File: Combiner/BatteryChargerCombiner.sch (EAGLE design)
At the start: 148 parts, among them Q1 DMN6040SSD-13, Q2 DMN6040SSD-13, Q3 DMN6040SSD-13, Q4 DMN6040SSD-13, Q5 DMP4047SSD-13, Q6 220mA/50V/3.5Ω, Q7 220mA/50V/3.5Ω, U1 BQ24650, U10 TS7211, U11 MIC5219 3.3V, U12 MKR1000-SMD, U13 STWD100, U2 BQ28Z610, U3 BQ28Z610, U4 BQ24650, U5 TCA9543A, U6 WE-78, U7 WE-78, U8 74AHC1G07DBV, U9 74AUC1G06DBV

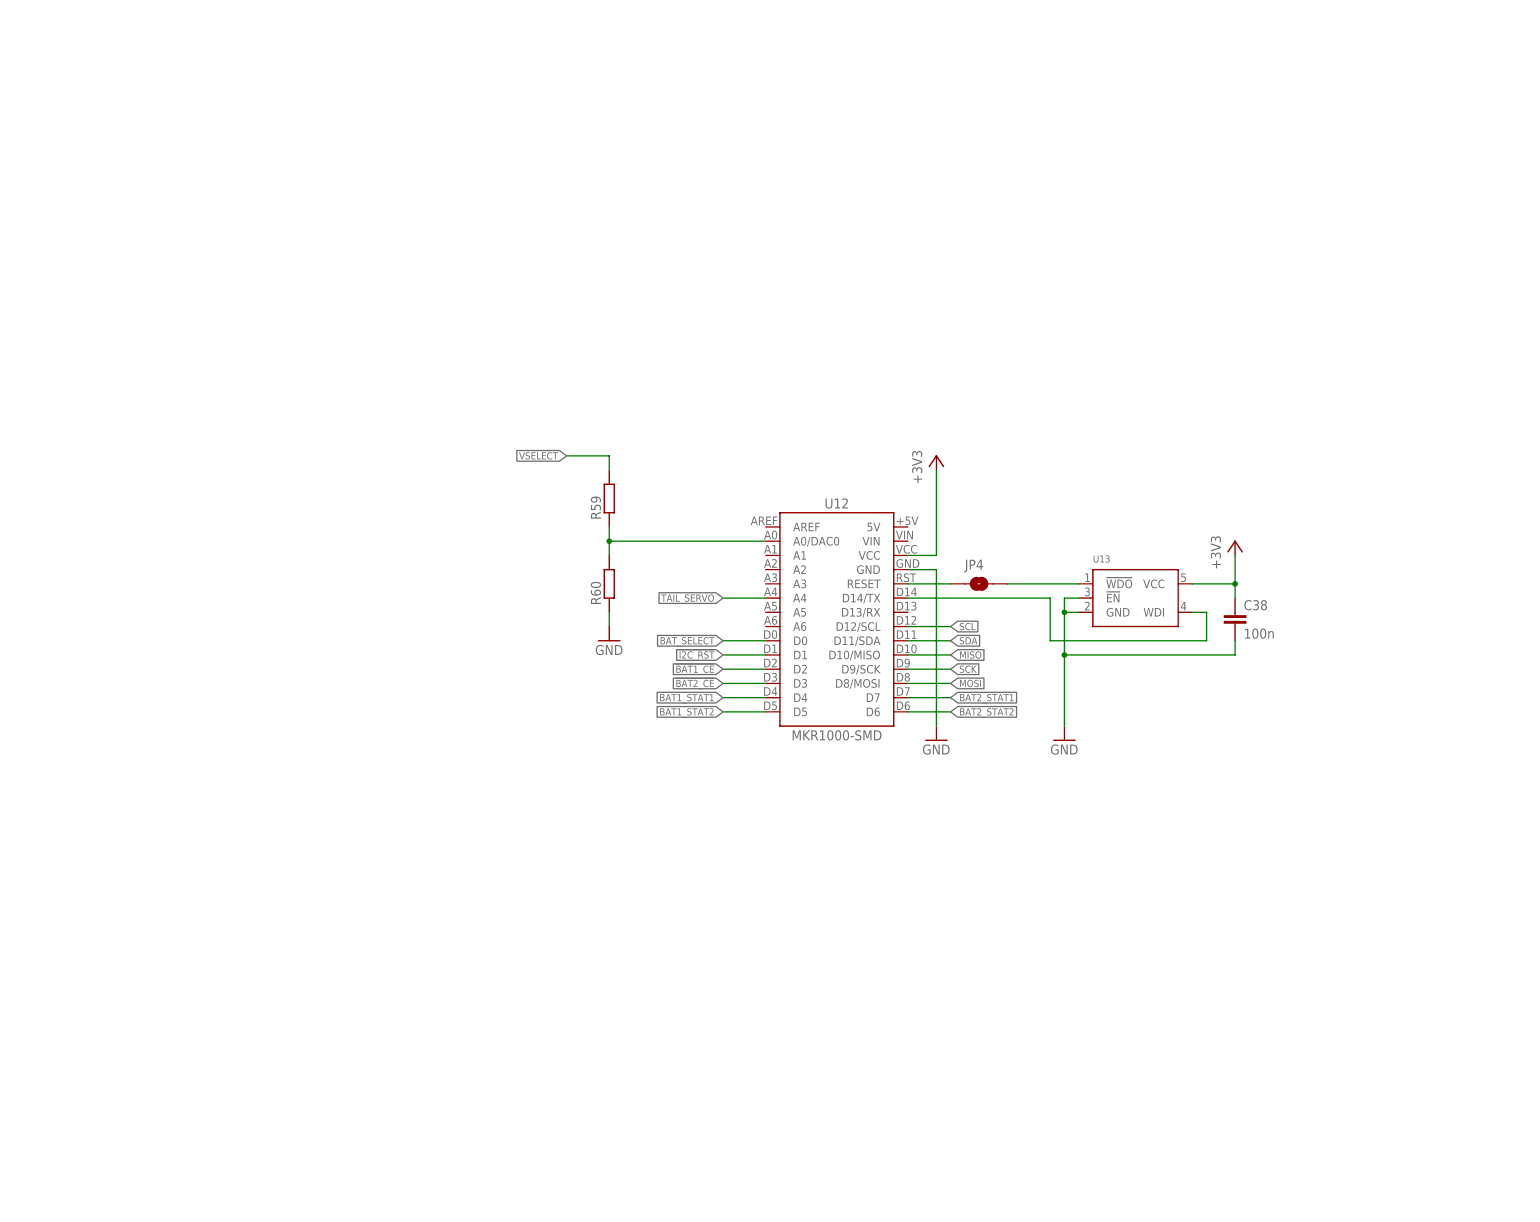
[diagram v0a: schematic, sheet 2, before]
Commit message: Added temp sensor inputs, power switches, and mounting holes
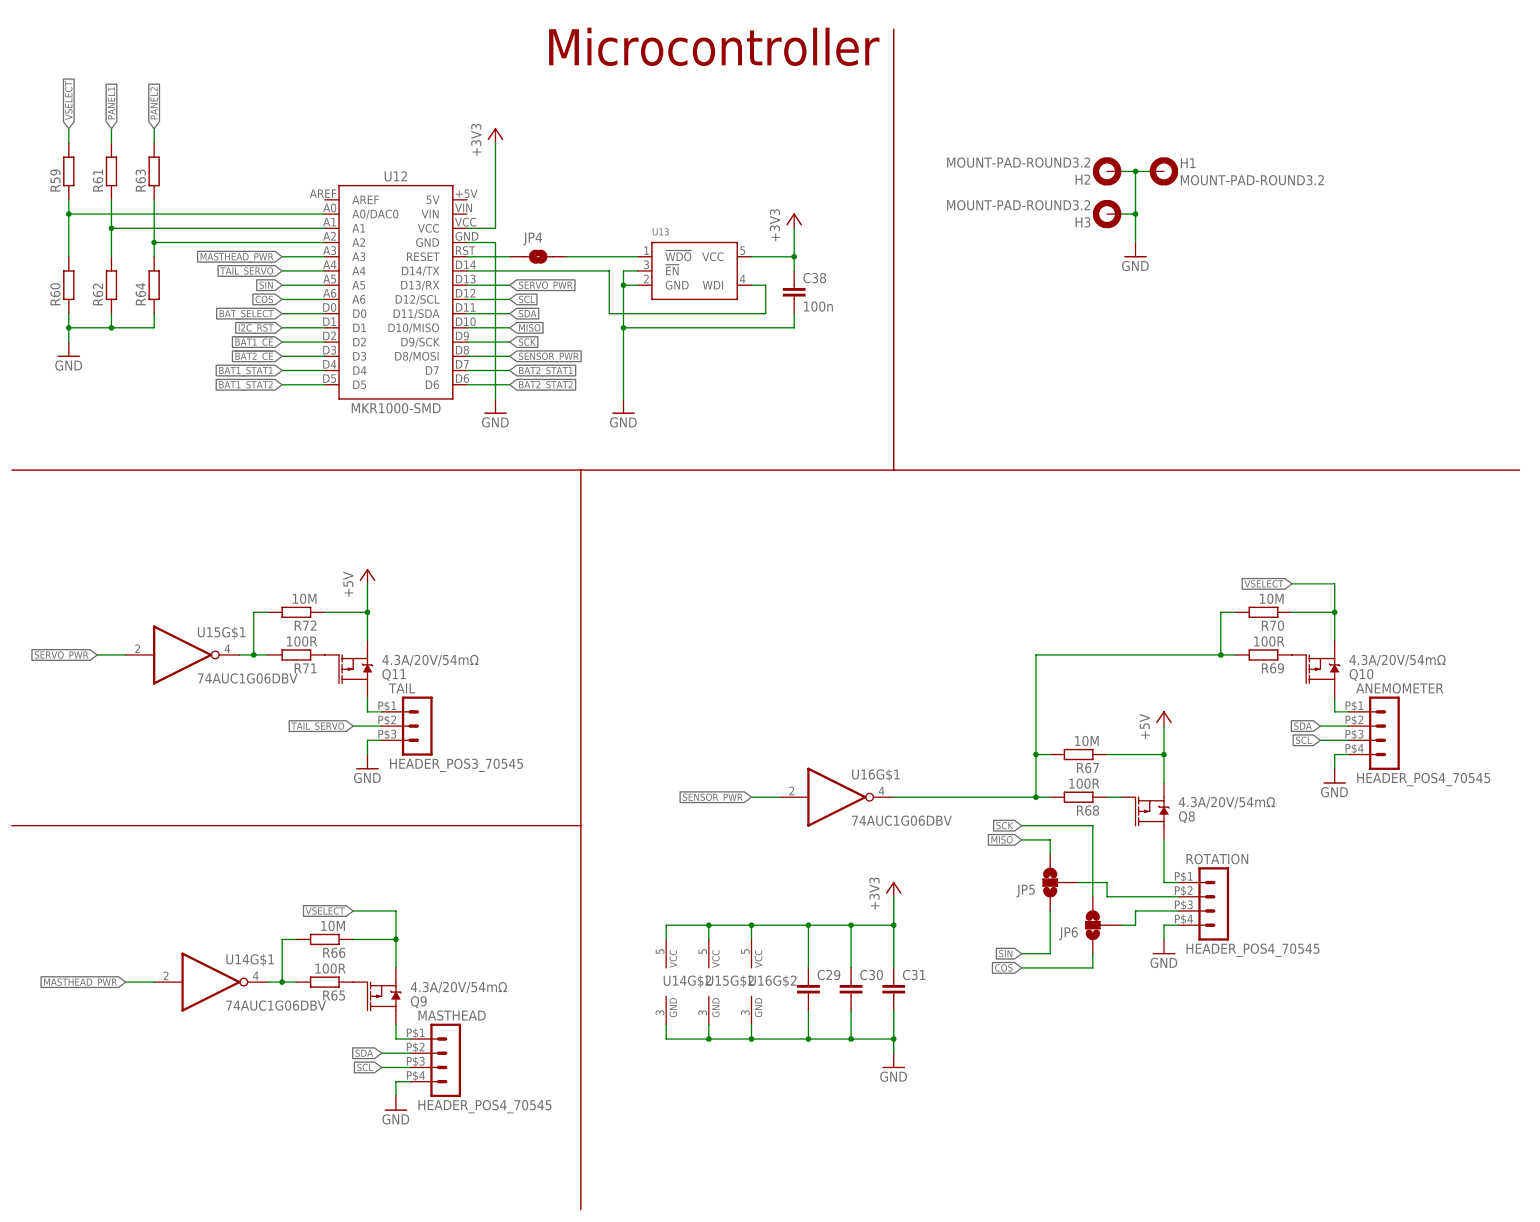
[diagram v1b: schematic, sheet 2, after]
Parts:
- removed JP3: JUMPER-SMT_3_NO_SILK, SparkFun-Jumpers:JUMPER-SMT_3_NO_SILK
- added C29, C30, C31: (no value), resistor:C-EUC0603
- added H1, H2, H3: MOUNT-PAD-ROUND3.2, holes:MOUNT-PAD-ROUND3.2
- added JP5, JP6: JUMPER-SMT_3_NO_SILK, SparkFun-Jumpers:JUMPER-SMT_3_NO_SILK
- added MASTHEAD: HEADER_POS4_70545, con-molex-c-grid-sl:HEADER_POS4_70545
- added Q10, Q11, Q8, Q9: 4.3A/20V/54mΩ, SparkFun-DiscreteSemi:MOSFET_PCH-IRLML2244
- added R61, R62, R63, R64: (no value), resistor:R-EU_R0603
- added R65, R68, R69, R71: 100R, resistor:R-EU_R0603
- added R66, R67, R70, R72: 10M, resistor:R-EU_R0603
- added U14, U15, U16: 74AUC1G06DBV, 74xx-little-us:74AUC1G06DBV
- BAT1_TS, BAT2_TS: value TPPAD1-13Y -> HEADER_POS3_70545; device testpad:TPPAD1-13Y -> con-molex-c-grid-sl:HEADER_POS3_70545
- ROTATION: value HEADER_POS5_70545 -> HEADER_POS4_70545; device con-molex-c-grid-sl:HEADER_POS5_70545 -> con-molex-c-grid-sl:HEADER_POS4_70545
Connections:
- removed net BAT1_TS: U2.TS1
- removed net BAT2_TS: U3.TS1
- removed net MOSI: ROTATION.2, U12.D8/MOSI
- removed net TS1: BAT1_TS.TP, R5.1, R6.2, U1.TS
- removed net TS2: BAT2_TS.TP, R16.1, R17.2, U4.TS
- new net BAT1_TS1: BAT1_TS.1, R5.1, R6.2, U1.TS
- new net BAT1_TS2: BAT1_TS.2, U2.TS1
- new net BAT2_TS1: BAT2_TS.1, R16.1, R17.2, U4.TS
- new net BAT2_TS2: BAT2_TS.2, U3.TS1
- new net COS: JP6.1, U12.A6
- new net MASTHEAD_PWR: U12.A3, U14G$1.I
- new net N$47: JP6.2, ROTATION.3
- new net N$49: JP5.2, ROTATION.2
- new net N$53: Q8.G, R68.1
- new net N$56: R63.1, R64.2, U12.A2
- new net N$58: MASTHEAD.1, Q9.D
- new net N$63: Q9.G, R65.1
- new net N$66: ANEMOMETER.1, Q10.D
- new net N$67: Q10.G, R69.1
- new net N$69: R67.2, R68.2, R69.2, R70.2, U16G$1.O
- new net N$70: Q11.D, TAIL.1
- new net N$71: Q11.G, R71.1
- new net N$72: R71.2, R72.2, U15G$1.O
- new net PANEL1: D1.A, PANEL1_POS.TP, R1.2, R61.2
- new net PANEL2: D2.A, PANEL2_POS.TP, R13.2, R63.2
- new net SENSOR_PWR: U12.D8/MOSI, U16G$1.I
- new net SERVO_PWR: U12.D13/RX, U15G$1.I
- new net SIN: JP5.1, U12.A5
- net +3V3: now also C29.1, C30.1, C31.1, U14G$2.VCC, U15G$2.VCC, U16G$2.VCC; no longer JP3.1
- net +5V: now also Q11.S, Q8.S, R67.1, R72.1; no longer JP3.3, TAIL.1
- net GND: now also BAT1_TS.3, BAT2_TS.3, C29.2, C30.2, C31.2, H1.MOUNT, H2.MOUNT, H3.MOUNT, MASTHEAD.4, R62.1, R64.1, ROTATION.4, U14G$2.GND, U15G$2.GND, U16G$2.GND; no longer ROTATION.5
- net MISO: now also JP5.3; no longer ROTATION.4
- net N$14: now also R61.1, R62.2, U12.A1; no longer D2.A, PANEL2_POS.TP, R13.2
- net N$2: now also Q8.D, ROTATION.1; no longer D1.A, PANEL1_POS.TP, R1.2
- net N$64: now also R65.2, R66.2, U14G$1.O; no longer JP3.2, ROTATION.1
- net SCK: now also JP6.3; no longer ROTATION.3
- net SCL: now also MASTHEAD.3
- net SDA: now also MASTHEAD.2
- net VSELECT: now also Q10.S, Q9.S, R66.1, R70.1; no longer ANEMOMETER.1
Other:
- note added: "Microcontroller"
- moved on the sheet: BAT1, BAT2, C38, JP4, PANEL1_NEG, PANEL1_POS, PANEL2_NEG, PANEL2_POS, PWR_OUT, R59, R60, U12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

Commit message: Silkscreen cleaned up; ready for test
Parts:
- removed JP4: JUMPER-SMT_2_NO_SILK, SparkFun-Jumpers:JUMPER-SMT_2_NO_SILK
- removed JP5, JP6: JUMPER-SMT_3_NO_SILK, SparkFun-Jumpers:JUMPER-SMT_3_NO_SILK
- added C32: 100n, resistor:C-EUC0603
- added R73, R74, R75, R76, R77, R78: (no value), resistor:R-EU_R0603
- added U17: LMV358, SparkFun-IC-Amplifiers:LMV358SOIC
- added WDT-RST: JUMPER-SMT_2_NO_SILK, SparkFun-Jumpers:JUMPER-SMT_2_NO_SILK
- C29, C30, C31: value (none) -> 100n
- SYSTEM: value HEADER_POS14_70545 -> HEADER_POS15_70545; device con-molex-c-grid-sl:HEADER_POS14_70545 -> con-molex-c-grid-sl:HEADER_POS15_70545
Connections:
- removed net N$14: R61.1, R62.2, U12.A1
- removed net N$47: JP6.2, ROTATION.3
- removed net N$49: JP5.2, ROTATION.2
- removed net N$56: R63.1, R64.2, U12.A2
- new net COS_IN: R75.2, ROTATION.3
- new net N$62: R73.1, R74.2, U17G1.-IN
- new net N$73: R75.1, R76.2, U17G2.-IN
- new net N$78: R77.1, R78.2, U17G1.+IN, U17G2.+IN
- new net PANEL1_DIV: R61.1, R62.2, SYSTEM.13, U12.A1
- new net PANEL2_DIV: R63.1, R64.2, SYSTEM.14, U12.A2
- new net SIN_IN: R73.2, ROTATION.2
- net +3V3: now also C32.1, R77.2, U17G3.P$V+
- net COS: now also R76.1, U17G2.OUT; no longer JP6.1
- net GND: now also C32.2, R78.1, SYSTEM.15, U17G3.P$V-; no longer SYSTEM.13, SYSTEM.14
- net MISO: no longer JP5.3
- net N$61: now also WDT-RST.1; no longer JP4.1
- net N$65: now also WDT-RST.2; no longer JP4.2
- net SCK: no longer JP6.3
- net SIN: now also R74.1, U17G1.OUT; no longer JP5.1
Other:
- note added: "Masthead Light"
- note added: "Power & Ground"
- note added: "Sensor Inputs"
- note added: "Tail Servo"
- moved on the sheet: ANEMOMETER, C29, C30, C31, C38, H1, H2, H3, Q10, Q8, R59, R60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

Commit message: Now with selectable control schemes for the masthead light -- either I2C or PWM dimming & Neopixel
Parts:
- added JP3, JP4: JUMPER-SMT_3_NO_SILK, SparkFun-Jumpers:JUMPER-SMT_3_NO_SILK
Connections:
- removed net MISO: U12.D10/MISO
- removed net SCK: U12.D9/SCK
- new net DIM: JP4.3, U12.D10/MISO
- new net N$14: JP3.2, MASTHEAD.2
- new net N$47: JP4.2, MASTHEAD.3
- new net NEOPIXEL: JP3.3, U12.D9/SCK
- net SCL: now also JP3.1; no longer MASTHEAD.3
- net SDA: now also JP4.1; no longer MASTHEAD.2
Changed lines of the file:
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@@
 <part name="+3V10" library="supply1" library_urn="urn:adsk.eagle:library:371" deviceset="+3V3" device=""/>
 <part name="GND44" library="supply1" library_urn="urn:adsk.eagle:library:371" deviceset="GND" device=""/>
+<part name="JP3" library="SparkFun-Jumpers" library_urn="urn:adsk.eagle:library:528" deviceset="JUMPER-SMT_3_NO" device="_SILK" package3d_urn="urn:adsk.eagle:package:39285/1"/>
+<part name="JP4" library="SparkFun-Jumpers" library_urn="urn:adsk.eagle:library:528" deviceset="JUMPER-SMT_3_NO" device="_SILK" package3d_urn="urn:adsk.eagle:package:39285/1"/>
 </parts>
 <sheets>
@@
 <instance part="+3V10" gate="G$1" x="248.92" y="71.12"/>
 <instance part="GND44" gate="1" x="248.92" y="40.64"/>
+<instance part="JP3" gate="G$1" x="35.56" y="25.4" smashed="yes" rot="R180">
+<attribute name="NAME" x="33.02" y="25.019" size="1.778" layer="95" font="vector" rot="R180"/>
+</instance>
+<instance part="JP4" gate="G$1" x="50.8" y="15.24" smashed="yes" rot="R180">
+<attribute name="NAME" x="48.26" y="14.859" size="1.778" layer="95" font="vector" rot="R180"/>
+</instance>
 </instances>
 <busses>
@@
 </segment>
 <segment>
-<pinref part="MASTHEAD" gate="G$1" pin="2"/>
-<wire x1="76.2" y1="27.94" x2="71.12" y2="27.94" width="0.1524" layer="91"/>
-<label x="71.12" y="27.94" size="1.27" layer="95" rot="R180" xref="yes"/>
+<pinref part="JP4" gate="G$1" pin="1"/>
+<wire x1="50.8" y1="10.16" x2="50.8" y2="7.62" width="0.1524" layer="91"/>
+<wire x1="50.8" y1="7.62" x2="45.72" y2="7.62" width="0.1524" layer="91"/>
+<label x="45.72" y="7.62" size="1.27" layer="95" rot="R180" xref="yes"/>
 </segment>
 </net>
@@
 </segment>
 <segment>
-<pinref part="MASTHEAD" gate="G$1" pin="3"/>
-<wire x1="76.2" y1="25.4" x2="71.12" y2="25.4" width="0.1524" layer="91"/>
-<label x="71.12" y="25.4" size="1.27" layer="95" rot="R180" xref="yes"/>
+<pinref part="JP3" gate="G$1" pin="1"/>
+<wire x1="35.56" y1="20.32" x2="35.56" y2="17.78" width="0.1524" layer="91"/>
+<wire x1="35.56" y1="17.78" x2="30.48" y2="17.78" width="0.1524" layer="91"/>
+<label x="30.48" y="17.78" size="1.27" layer="95" rot="R180" xref="yes"/>
 </segment>
 </net>
@@
 </segment>
 </net>
-<net name="SCK" class="0">
+<net name="NEOPIXEL" class="0">
 <segment>
 <pinref part="U12" gate="G$1" pin="D9/SCK"/>
@@
 <label x="104.14" y="154.94" size="1.27" layer="95" xref="yes"/>
 </segment>
-</net>
-<net name="MISO" class="0">
+<segment>
+<pinref part="JP3" gate="G$1" pin="3"/>
+<wire x1="35.56" y1="30.48" x2="35.56" y2="33.02" width="0.1524" layer="91"/>
+<wire x1="35.56" y1="33.02" x2="30.48" y2="33.02" width="0.1524" layer="91"/>
+<label x="30.48" y="33.02" size="1.27" layer="95" rot="R180" xref="yes"/>
+</segment>
+</net>
+<net name="DIM" class="0">
 <segment>
 <pinref part="U12" gate="G$1" pin="D10/MISO"/>
 <wire x1="96.52" y1="157.48" x2="104.14" y2="157.48" width="0.1524" layer="91"/>
 <label x="104.14" y="157.48" size="1.27" layer="95" xref="yes"/>
+</segment>
+<segment>
+<pinref part="JP4" gate="G$1" pin="3"/>
+<wire x1="50.8" y1="20.32" x2="50.8" y2="22.86" width="0.1524" layer="91"/>
+<wire x1="50.8" y1="22.86" x2="45.72" y2="22.86" width="0.1524" layer="91"/>
+<label x="45.72" y="22.86" size="1.27" layer="95" rot="R180" xref="yes"/>
 </segment>
 </net>
@@
 </segment>
 </net>
+<net name="N$14" class="0">
+<segment>
+<pinref part="MASTHEAD" gate="G$1" pin="2"/>
+<pinref part="JP3" gate="G$1" pin="2"/>
+<wire x1="40.64" y1="25.4" x2="43.18" y2="25.4" width="0.1524" layer="91"/>
+<wire x1="43.18" y1="25.4" x2="43.18" y2="27.94" width="0.1524" layer="91"/>
+<wire x1="43.18" y1="27.94" x2="76.2" y2="27.94" width="0.1524" layer="91"/>
+</segment>
+</net>
+<net name="N$47" class="0">
+<segment>
+<pinref part="MASTHEAD" gate="G$1" pin="3"/>
+<pinref part="JP4" gate="G$1" pin="2"/>
+<wire x1="55.88" y1="15.24" x2="58.42" y2="15.24" width="0.1524" layer="91"/>
+<wire x1="58.42" y1="15.24" x2="58.42" y2="25.4" width="0.1524" layer="91"/>
+<wire x1="58.42" y1="25.4" x2="76.2" y2="25.4" width="0.1524" layer="91"/>
+</segment>
+</net>
